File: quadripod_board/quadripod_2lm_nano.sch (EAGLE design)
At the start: 8 parts

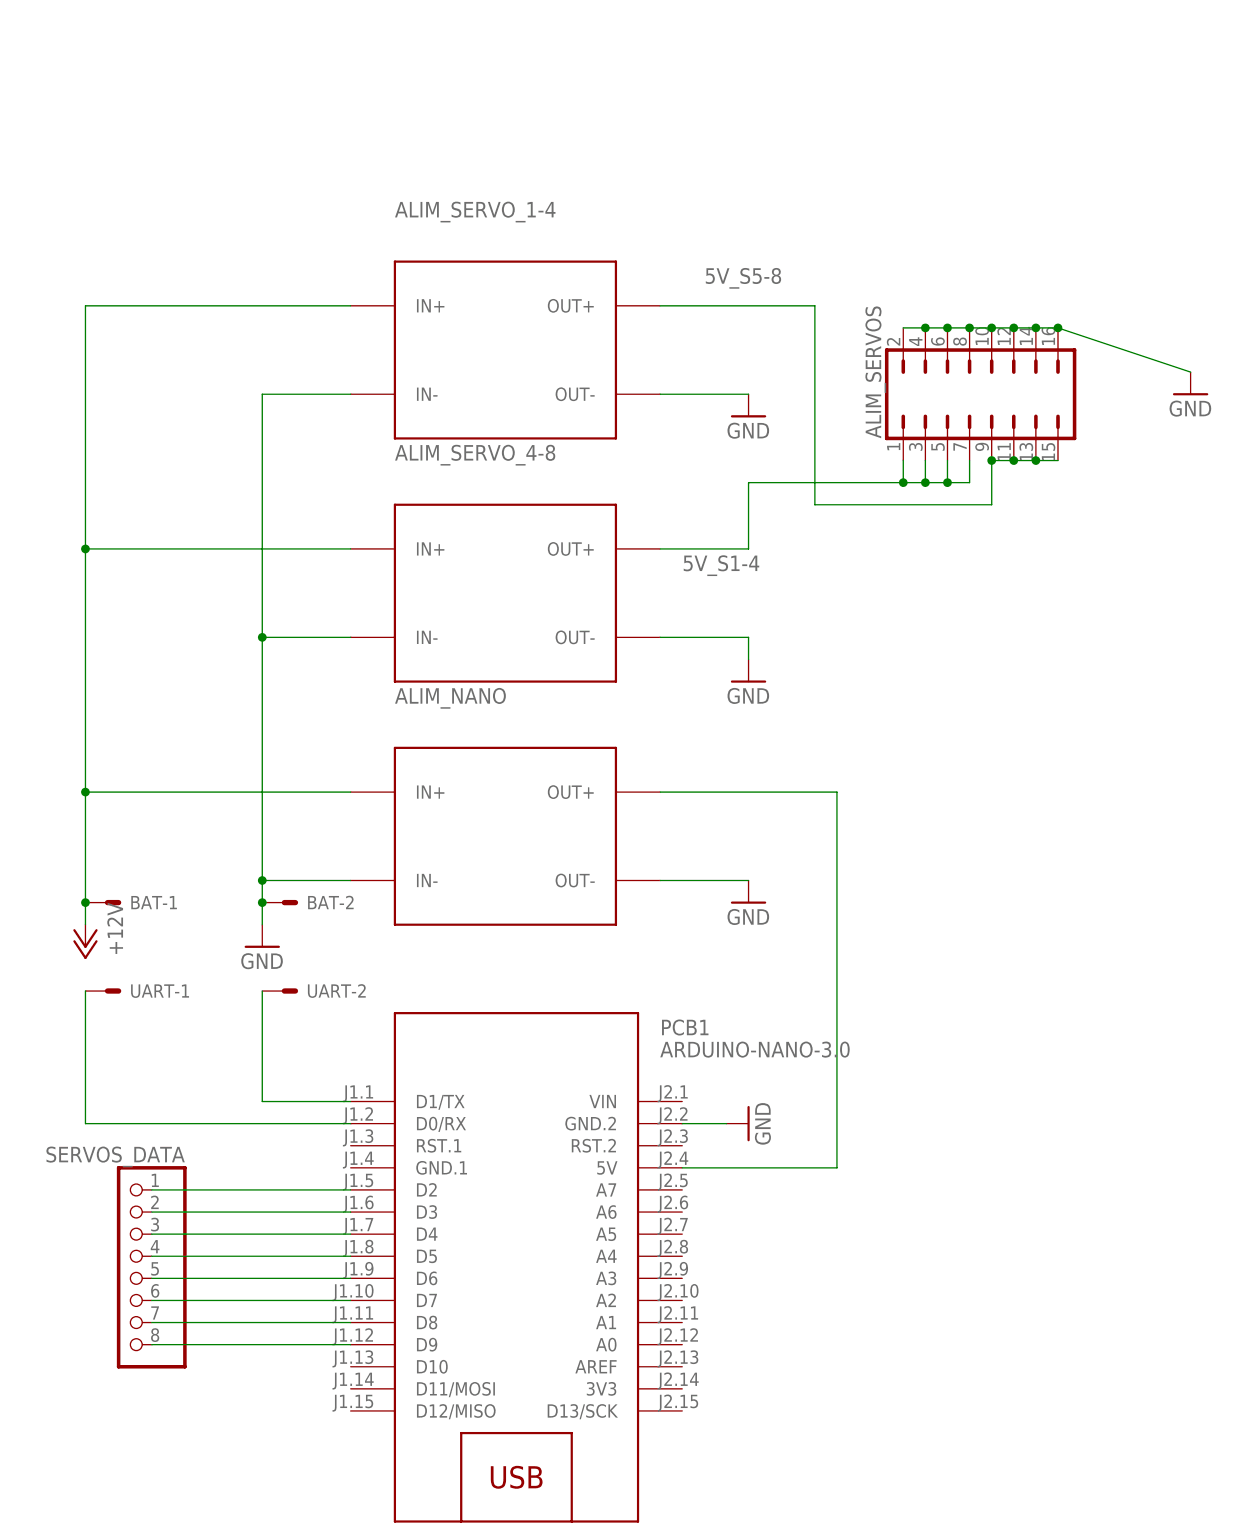
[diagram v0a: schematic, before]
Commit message: board revision, added diodes to avoid powering the servos while programming the arduino
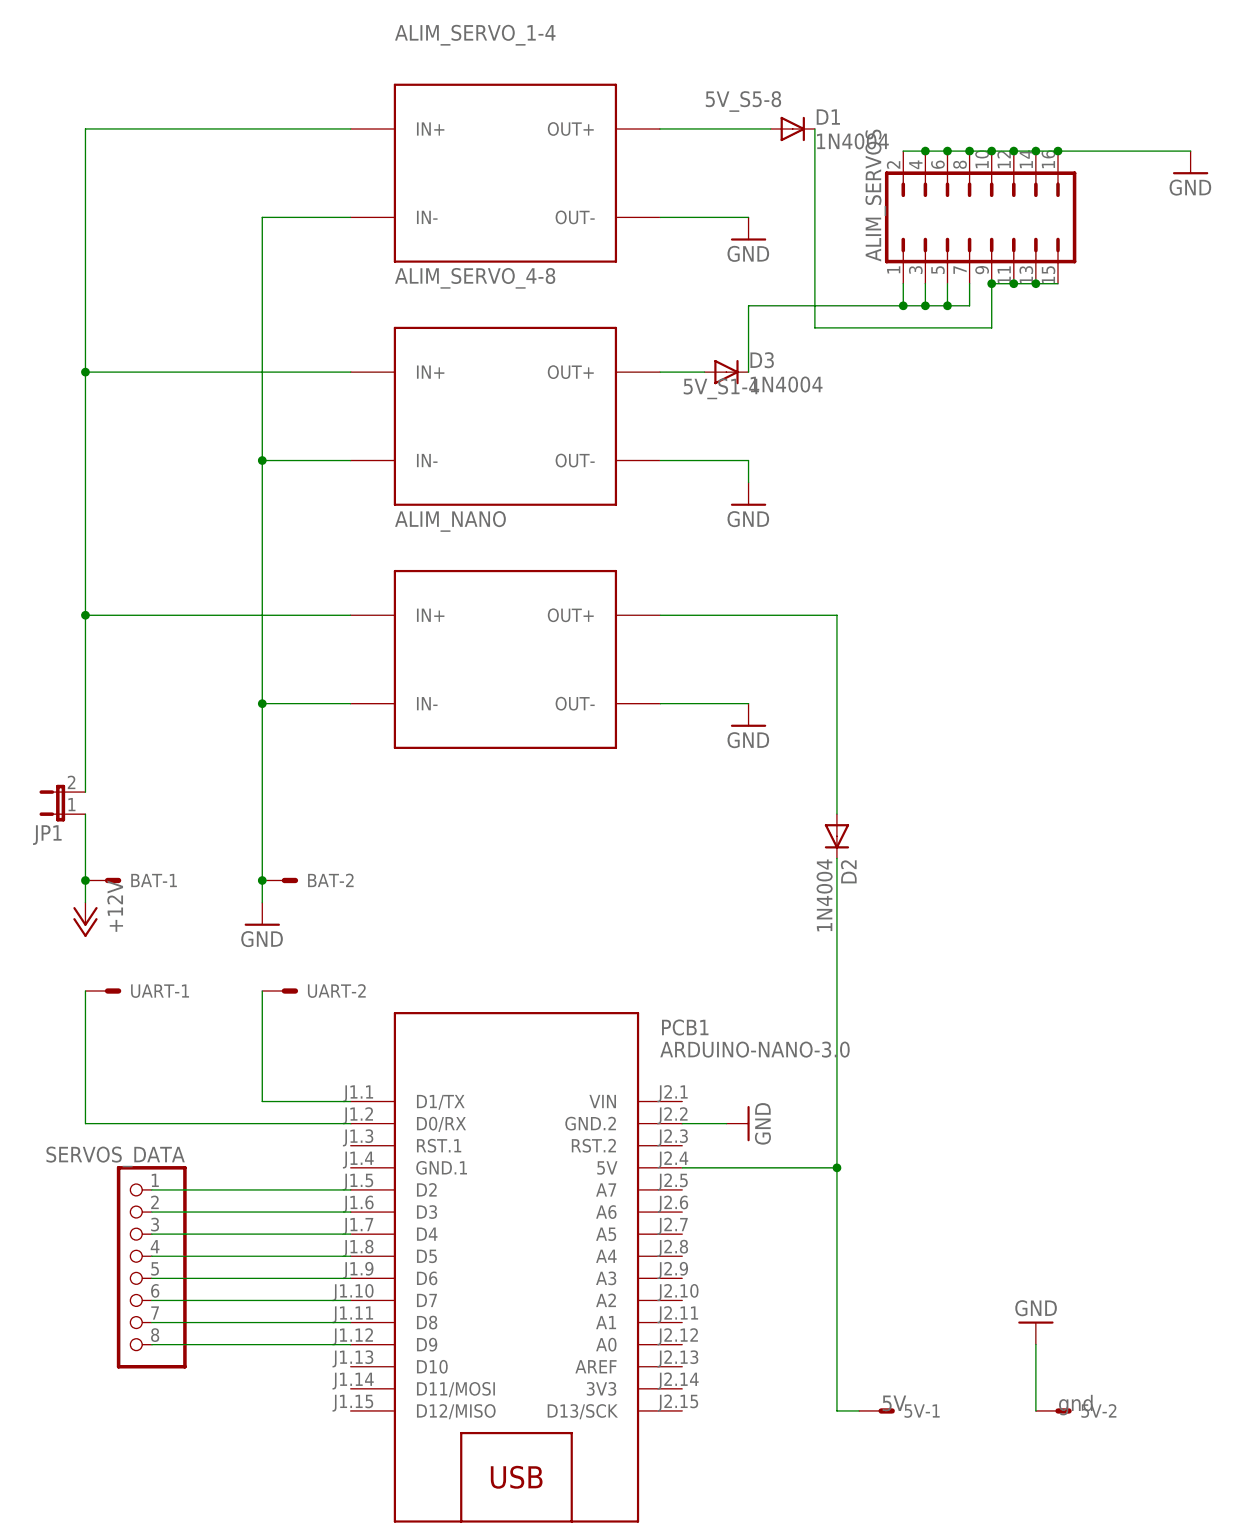
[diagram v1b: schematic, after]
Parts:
- added 5V: 332-02, con-garry:332-02
- added D1, D2, D3: 1N4004, diode:1N4004
- added JP1: (no value), jumper:JP1E
- BAT: VOLT (none) -> gnd; VOLTAGE (none) -> 12V
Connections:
- new net N$1: ALIM_SERVO_4-8.OUT+, D3.A
- new net N$15: ALIM_NANO.IN+, ALIM_SERVO_1-4.IN+, ALIM_SERVO_4-8.IN+, JP1.2
- new net N$3: 5V-1.S, D2.C, PCB1.5V
- new net N$4: ALIM_SERVO_1-4.OUT+, D1.A
- net +12V: now also JP1.1; no longer ALIM_NANO.IN+, ALIM_SERVO_1-4.IN+, ALIM_SERVO_4-8.IN+
- net 5V_NANO: now also D2.A; no longer PCB1.5V
- net 5V_S1-4: now also D3.C; no longer ALIM_SERVO_4-8.OUT+
- net 5V_S5-8: now also D1.C; no longer ALIM_SERVO_1-4.OUT+
- net GND: now also 5V-2.S
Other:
- moved on the sheet: ALIM_NANO, ALIM_SERVOS, ALIM_SERVO_1-4, ALIM_SERVO_4-8, BAT-1, BAT-2
